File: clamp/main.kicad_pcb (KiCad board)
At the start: 2 copper layers, 37 parts, among them P1 CONN_01X12, U1 LM741, U2 LM741, U3 LM741, U4 LM741, U5 LM741, U6 LM741

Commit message: basic layout
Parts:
- added C14: C, Capacitors_SMD:C_1206, F.Cu at (116.2, 55.9)
- added C15: C, Capacitors_SMD:C_1206, F.Cu at (132.7, 66.0)
- added C16: C, Capacitors_SMD:C_1206, F.Cu at (119.4, 74.9)
- added C17: C, Capacitors_SMD:C_1206, F.Cu at (63.5, 62.2)
- added C18: C, Capacitors_SMD:C_1206, F.Cu at (76.8, 72.4)
- added C19: C, Capacitors_SMD:C_1206, F.Cu at (76.8, 57.1)
- added C20: C, Capacitors_SMD:C_1206, F.Cu at (88.3, 61.6)
- added C21: C, Capacitors_SMD:C_1206, F.Cu at (91.4, 66.7)
- added C22: C, Capacitors_SMD:C_1206, F.Cu at (91.4, 72.4)
- added C23: C, Capacitors_SMD:C_1206, F.Cu at (93.3, 79.4)
- added C24: C, Capacitors_SMD:C_1206, F.Cu at (94.0, 84.5)
- added C25: C, Capacitors_SMD:C_1206, F.Cu at (88.3, 90.2)
- added C26: C, Capacitors_SMD:C_1206, F.Cu at (243.2, 57.8)
- added C27: C, Capacitors_SMD:C_1206, F.Cu at (241.3, 43.8)
- added C28: C, Capacitors_SMD:C_1206, F.Cu at (237.5, 43.8)
- added C33: C, Capacitors_SMD:C_1206, F.Cu at (252.7, 57.8)
- added C34: C, Capacitors_SMD:C_1206, F.Cu at (249.6, 57.8)
- added D5: 1N4148, Diodes_ThroughHole:Diode_DO-35_SOD27_Horizontal_RM10, F.Cu at (179.7, 38.1)
- added D6: 1N4148, Diodes_ThroughHole:Diode_DO-35_SOD27_Horizontal_RM10, F.Cu at (183.5, 48.3)
- added D7: 1N4148, Diodes_ThroughHole:Diode_DO-35_SOD27_Horizontal_RM10, F.Cu at (247.0, 43.2)
- added P2: CONN_01X15, Pin_Headers:Pin_Header_Straight_1x15, F.Cu at (56.5, 73.7)
- added P3: CONN_01X03, Pin_Headers:Pin_Header_Straight_1x03, F.Cu at (69.2, 33.0)
- added P4: CONN_01X06, Pin_Headers:Pin_Header_Straight_1x06, F.Cu at (221.6, 43.8)
- added R15: R, Resistors_SMD:R_1206, F.Cu at (121.9, 61.0)
- added R20: 120, Resistors_ThroughHole:Resistor_Vertical_RM5mm, F.Cu at (230.5, 49.5)
- added R21: R, Resistors_ThroughHole:Resistor_Vertical_RM5mm, F.Cu at (237.5, 33.0)
- added U13: LM741, SMD_Packages:SOIC-8-N, F.Cu at (246.4, 50.2)
- added U7: LM741, Housings_SOIC:SOIC-8_3.9x4.9mm_Pitch1.27mm, F.Cu at (123.2, 67.3)
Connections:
- C1 pad 1: -VE -> +VE
- C2 pad 1: +VE -> -VE
- D2 pad 1: Net-(D2-Pad1) -> OUT
- D2 pad 2: OUT -> Net-(D2-Pad2)
- D3 pad 1: OUT -> Net-(D3-Pad1)
- D3 pad 2: Net-(D3-Pad2) -> OUT
- R10 pad 2: V-FB -> I-FB
- R11 pad 1: Net-(R10-Pad1) -> Net-(R11-Pad1)
- R11 pad 2: V-SET -> V-FB
- R12 pad 1: Net-(R12-Pad1) -> Net-(R11-Pad1)
- R12 pad 2: V-FB -> Net-(R12-Pad2)
- R13 pad 1: Net-(R12-Pad1) -> OUT
- R13 pad 2: Net-(R13-Pad2) -> REF
- R14 pad 1: -VE -> Net-(R14-Pad1)
- R14 pad 2: +VE -> REF
- R2 pad 2: Net-(R1-Pad1) -> V-SET
- R3 pad 2: I-FB -> Net-(R1-Pad1)
- R4 pad 1: Net-(R3-Pad1) -> Net-(R12-Pad2)
- R4 pad 2: I-SET -> Net-(R2-Pad1)
- R6 pad 2: Net-(R2-Pad1) -> I-SET
- R7 pad 1: OUT -> Net-(R7-Pad1)
- R7 pad 2: REF -> V-FB
- R8 pad 1: Net-(R8-Pad1) -> Net-(R7-Pad1)
- R9 pad 1: Net-(R13-Pad2) -> Net-(R10-Pad1)
- R9 pad 2: Net-(R8-Pad1) -> Net-(R3-Pad1)
- U1 pad 2: OUT -> Net-(R1-Pad1)
- U1 pad 3: Net-(R3-Pad1) -> GND
- U1 pad 6: Net-(D1-Pad2) -> Net-(R3-Pad1)
- U2 pad 2: Net-(R1-Pad1) -> Net-(R2-Pad1)
- U2 pad 6: Net-(R2-Pad1) -> Net-(R12-Pad2)
- U3 pad 6: Net-(D2-Pad1) -> Net-(D1-Pad2)
- U4 pad 2: Net-(R8-Pad1) -> OUT
- U4 pad 3: GND -> Net-(R10-Pad1)
- U4 pad 6: Net-(R13-Pad2) -> Net-(D4-Pad1)
- U5 pad 3: Net-(R10-Pad1) -> Net-(R7-Pad1)
- U5 pad 6: Net-(D3-Pad2) -> Net-(D2-Pad2)
- U6 pad 3: Net-(R12-Pad1) -> Net-(R11-Pad1)
- U6 pad 6: Net-(D4-Pad1) -> Net-(D3-Pad1)
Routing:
- net V-FB: track 52.3 -> 0.07 mm
- net OUT: track 216.8 -> 183.7 mm
- net I-FB: track 36.9 -> 12.5 mm
- net I-SET: track 35.7 -> 12.4 mm
- net Net-(R13-Pad2): track 21.5 -> 0.00 mm
- net V-SET: track 43.3 -> 23.5 mm
- net -VE: track 270.8 -> 251.6 mm, vias 9 -> 8
- net Net-(R8-Pad1): track 16.0 -> 0.00 mm
- net Net-(R2-Pad1): track 13.9 -> 0.00 mm
- net Net-(R12-Pad1): track 10.1 -> 0.00 mm
- net +VE: track 292.1 -> 283.3 mm, vias 8 -> 7
- net Net-(D2-Pad2): track 0.00 -> 8.79 mm
- net Net-(R11-Pad1): track 0.00 -> 7.11 mm
- net Net-(R10-Pad1): track 10.8 -> 5.44 mm, vias 0 -> 1
- net Net-(R3-Pad1): track 9.36 -> 4.31 mm
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
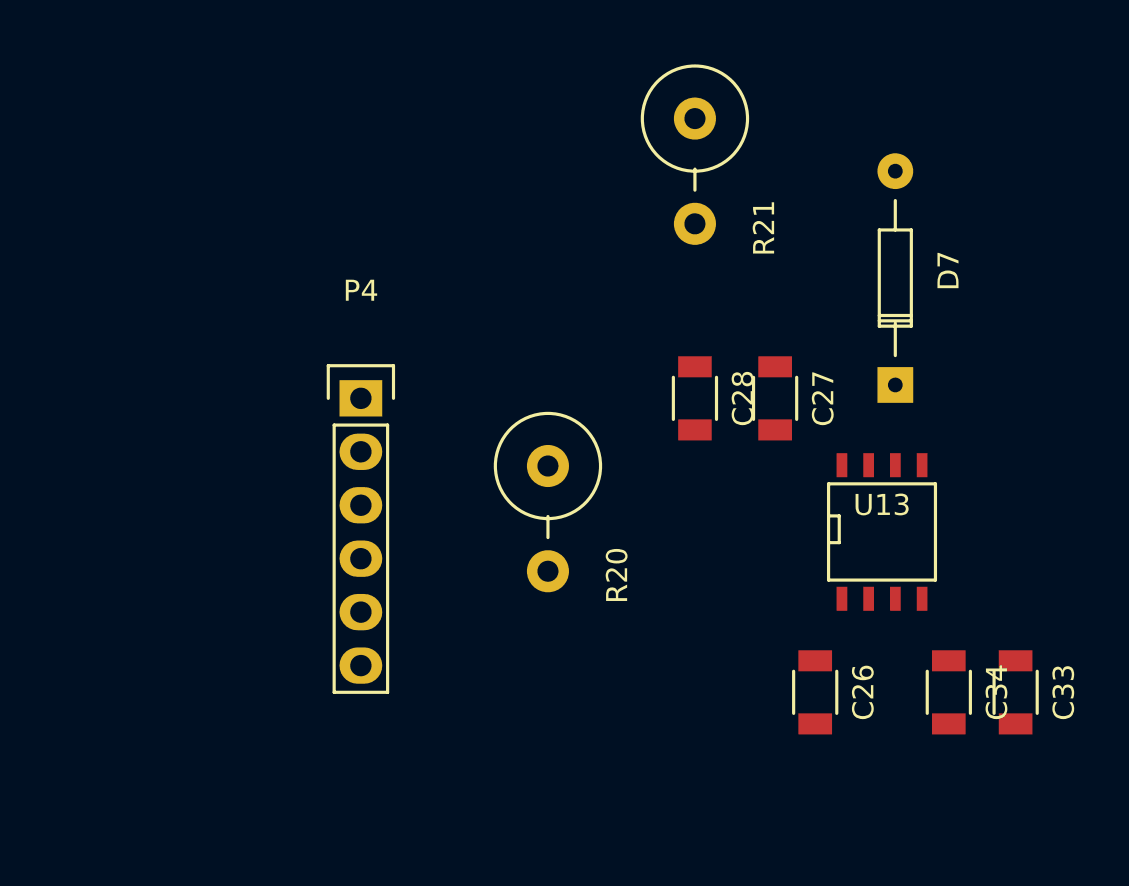
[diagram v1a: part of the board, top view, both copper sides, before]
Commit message: new footprint to-5
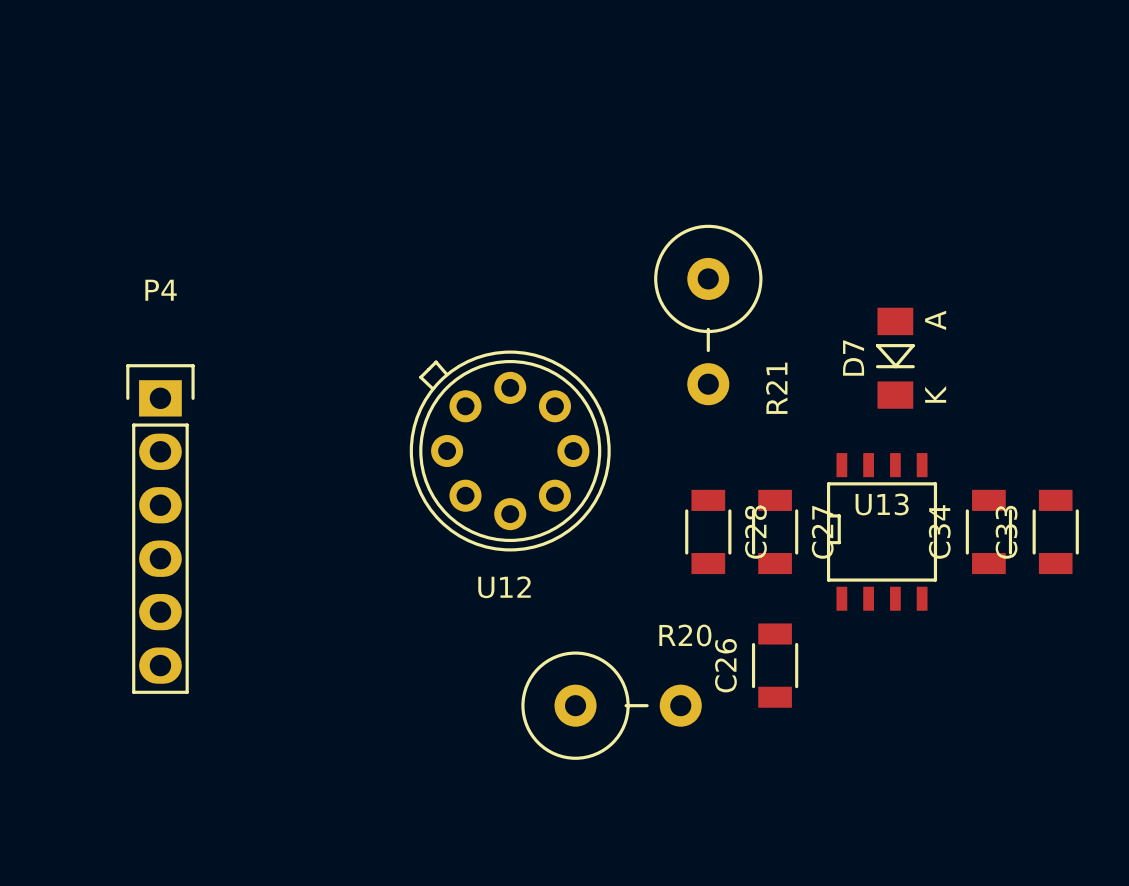
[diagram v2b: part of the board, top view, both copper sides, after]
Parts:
- added U12: LTZ1000, footprint:TO-5_Housing_8Pin, F.Cu at (228.6, 46.4)
- D7: footprint Diodes_ThroughHole:Diode_DO-35_SOD27_Horizontal_RM10 -> Diodes_SMD:MiniMELF_Standard
- moved R20 9.67 mm to (234.3, 58.4), turned to 0 degrees
- moved P4 9.53 mm to (212.1, 43.8)
- moved C33 7.85 mm to (254.6, 50.2), turned to 90 degrees
- moved C34 7.85 mm to (251.5, 50.2), turned to 90 degrees
- moved R21 7.65 mm to (238.1, 40.6)
- moved C28 6.38 mm to (238.1, 50.2)
- moved C27 6.35 mm to (241.3, 50.2)
- moved C26 2.29 mm to (241.3, 56.5), turned to 90 degrees
- moved D7 1.27 mm to (247.0, 41.9)

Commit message: pcb for first bit
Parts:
- R20, R21: footprint Resistors_ThroughHole:Resistor_Vertical_RM5mm -> Resistors_ThroughHole:Resistor_TO-220_Vertical
- moved R21 22.7 mm to (215.9, 45.1)
- moved R20 14.7 mm to (219.7, 57.1), turned to 270 degrees
- moved C26 4.49 mm to (245.7, 57.1), turned to 180 degrees
- moved P4 2.54 mm to (209.6, 43.8)
- turned U12 to 90 degrees
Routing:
- net GND: track 45.5 -> 152.6 mm, vias 8 -> 12
- net -VE: track 251.6 -> 325.3 mm, vias 8 -> 9
- net Net-(C26-Pad1): track 0.00 -> 71.0 mm
- net REF: track 0.69 -> 54.6 mm
- net +VE: track 283.3 -> 331.3 mm, vias 7 -> 8
- net Net-(R20-Pad1): track 0.00 -> 34.4 mm
- net Net-(D7-Pad1): track 0.00 -> 3.33 mm

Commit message: update
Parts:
- added C29: 0.1uF, Capacitors_SMD:C_1206, F.Cu at (187.3, 60.3)
- added C30: 0.1uF, Capacitors_SMD:C_1206, F.Cu at (207.6, 57.8)
- added D8: 1N4148, Diodes_SMD:MiniMELF_Standard, F.Cu at (211.5, 57.8)
- added Q1: 2N3904, TO_SOT_Packages_SMD:SOT-23, F.Cu at (186.7, 47.6)
- added R22: 1k, Resistors_SMD:R_1206, F.Cu at (192.4, 46.4)
- added R23: 1M, Resistors_SMD:R_1206, F.Cu at (192.4, 59.7)
- added R24: 10k, Resistors_SMD:R_1206, F.Cu at (196.2, 45.7)
- added RV1: POT, Potentiometers:Potentiometer_Bourns_3296Y_3-8Zoll_Angular_ScrewUp, F.Cu at (201.9, 47.0)
- added U14: LM741, SMD_Packages:SOIC-8-N, F.Cu at (193.0, 52.7)
- added r1: 70k, Resistors_ThroughHole:Resistor_TO-220_Vertical, F.Cu at (215.3, 46.4)
- C26: value C -> 22nF
- R21: value R -> 70k
- moved C33 56.6 mm to (198.1, 52.7)
- moved C28 50.2 mm to (188.0, 52.7)
- moved D5 47.0 mm to (132.7, 38.7)
- moved D6 45.1 mm to (138.4, 48.9)
- moved P4 11.9 mm to (214.6, 33.0), turned to 270 degrees
- moved R21 7.73 mm to (208.3, 46.4)
- moved R20 4.45 mm to (215.3, 57.1)
- moved C27 3.18 mm to (238.1, 50.2)
- turned U12 to 270 degrees
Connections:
- R21 pad 2: Net-(C26-Pad1) -> Net-(C30-Pad1)
- U12 pad 1: (no net) -> Net-(C29-Pad2)
- U12 pad 2: (no net) -> Net-(D8-Pad1)
- U12 pad 6: (no net) -> Net-(R24-Pad2)
- U12 pad 8: (no net) -> Net-(C30-Pad1)
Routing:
- net -VE: track 325.3 -> 420.3 mm, vias 9 -> 11
- net +VE: track 331.3 -> 390.2 mm, vias 8 -> 10
- net GND: track 152.6 -> 205.8 mm, vias 12 -> 20
- net Net-(C30-Pad1): track 0.00 -> 44.2 mm
- net Net-(R24-Pad2): track 0.00 -> 32.6 mm
- net REF: track 54.6 -> 77.4 mm, vias 0 -> 2
- net Net-(R23-Pad1): track 0.00 -> 13.8 mm
- net Net-(C26-Pad1): track 71.0 -> 57.5 mm
- net Net-(C29-Pad2): track 0.00 -> 13.3 mm
- net Net-(C29-Pad1): track 0.00 -> 3.92 mm
- net Net-(Q1-Pad2): track 0.00 -> 3.40 mm
- net Net-(R22-Pad1): track 0.00 -> 3.25 mm
- net Net-(R20-Pad1): track 34.4 -> 32.1 mm
- net (no net): track 0.00 -> 1.80 mm

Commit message: update
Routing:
- net Net-(D8-Pad1): track 0.00 -> 20.1 mm
- net GND: track 205.8 -> 209.5 mm, vias 20 -> 19
- net Net-(C26-Pad1): track 57.5 -> 59.5 mm

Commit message: update
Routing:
- net Net-(C29-Pad2): track 13.3 -> 59.6 mm
- net Net-(D8-Pad1): track 20.1 -> 0.15 mm
- net +VE: track 390.0 -> 393.5 mm
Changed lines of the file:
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@@
   (general
     (links 167)
-    (no_connects 86)
+    (no_connects 87)
     (area 51.181667 26.645 257.270002 151.352002)
     (thickness 1.6)
     (drawings 13)
-    (tracks 478)
+    (tracks 490)
     (zones 0)
     (modules 76)
@@
   )
   (segment (start 181.61 40.005) (end 180.34 41.275) (width 0.75) (layer B.Cu) (net 0))
-  (segment (start 240.03 46.355) (end 240.03 48.665) (width 0.75) (layer F.Cu) (net 1))
+  (segment (start 237.49 40.005) (end 244.475 40.005) (width 0.75) (layer B.Cu) (net 1))
+  (segment (start 245.379998 45.72) (end 246.014998 46.355) (width 0.75) (layer F.Cu) (net 1))
+  (segment (start 245.11 45.72) (end 245.379998 45.72) (width 0.75) (layer F.Cu) (net 1))
+  (segment (start 244.475 45.085) (end 245.11 45.72) (width 0.75) (layer F.Cu) (net 1))
+  (segment (start 244.475 42.545) (end 244.475 45.085) (width 0.75) (layer F.Cu) (net 1))
+  (via (at 244.475 42.545) (size 1.75) (drill 0.75) (layers F.Cu B.Cu) (net 1))
+  (segment (start 244.475 40.005) (end 244.475 42.545) (width 0.75) (layer B.Cu) (net 1))
   (segment (start 240.03 48.665) (end 240.03 48.895) (width 0.75) (layer F.Cu) (net 1))
   (segment (start 240.03 48.895) (end 240.03 48.665) (width 0.75) (layer F.Cu) (net 1))
@@
   (segment (start 213.36 40.005) (end 213.995 40.005) (width 0.75) (layer B.Cu) (net 1))
   (segment (start 213.995 40.005) (end 237.49 40.005) (width 0.75) (layer B.Cu) (net 1))
-  (segment (start 237.49 40.005) (end 240.03 40.64) (width 0.75) (layer B.Cu) (net 1))
-  (segment (start 240.03 40.64) (end 240.03 46.355) (width 0.75) (layer B.Cu) (net 1))
-  (via (at 240.03 46.355) (size 1.75) (drill 0.75) (layers F.Cu B.Cu) (net 1))
   (segment (start 213.36 40.005) (end 214.63 33.02) (width 0.75) (layer B.Cu) (net 1) (status 20))
   (segment (start 245.745 48.895) (end 241.53 48.895) (width 0.75) (layer F.Cu) (net 1))
@@
   (segment (start 219.4075 44.1175) (end 217.805 45.72) (width 0.75) (layer F.Cu) (net 33))
   (segment (start 196.215 44.45) (end 196.215 44.27) (width 0.75) (layer F.Cu) (net 33))
+  (segment (start 228.6 57.785) (end 211.455 57.785) (width 0.75) (layer F.Cu) (net 34))
+  (segment (start 189.865 58.42) (end 191.135 59.69) (width 0.75) (layer F.Cu) (net 34))
+  (segment (start 191.135 59.69) (end 201.93 59.69) (width 0.75) (layer F.Cu) (net 34))
+  (segment (start 201.93 59.69) (end 203.2 60.96) (width 0.75) (layer F.Cu) (net 34))
+  (segment (start 203.2 60.96) (end 208.915 60.96) (width 0.75) (layer F.Cu) (net 34))
+  (segment (start 208.915 60.96) (end 209.55 60.325) (width 0.75) (layer F.Cu) (net 34))
+  (segment (start 209.55 60.325) (end 209.55 58.42) (width 0.75) (layer F.Cu) (net 34))
+  (segment (start 209.55 58.42) (end 210.185 57.785) (width 0.75) (layer F.Cu) (net 34))
+  (segment (start 210.185 57.785) (end 211.455 57.785) (width 0.75) (layer F.Cu) (net 34))
+  (segment (start 189.865 58.42) (end 185.825 58.42) (width 0.75) (layer F.Cu) (net 34))
   (segment (start 187.69076 48.575) (end 187.05576 48.575) (width 0.75) (layer F.Cu) (net 34))
   (segment (start 187.05576 48.575) (end 185.78576 49.845) (width 0.75) (layer F.Cu) (net 34))
@@
   (segment (start 185.78576 49.79924) (end 186.055 49.53) (width 0.75) (layer F.Cu) (net 34))
   (segment (start 185.78576 49.845) (end 185.78576 53.60924) (width 0.75) (layer F.Cu) (net 34))
-  (segment (start 185.825 54.205) (end 185.825 60.325) (width 0.75) (layer F.Cu) (net 34))
+  (segment (start 185.825 54.205) (end 185.825 58.42) (width 0.75) (layer F.Cu) (net 34))
+  (segment (start 185.825 58.42) (end 185.825 60.325) (width 0.75) (layer F.Cu) (net 34))
   (segment (start 185.78576 53.60924) (end 185.825 54.205) (width 0.75) (layer F.Cu) (net 34))
   (segment (start 211.455 56.03494) (end 211.60994 56.03494) (width 0.75) (layer F.Cu) (net 35))
-  (segment (start 211.60994 56.03494) (end 212.725 57.15) (width 0.75) (layer F.Cu) (net 35))
-  (segment (start 212.725 57.15) (end 231.14 57.15) (width 0.75) (layer F.Cu) (net 35))
   (segment (start 226.4375 48.3675) (end 218.5475 48.3675) (width 0.75) (layer F.Cu) (net 36))
   (segment (start 209.55 46.99) (end 208.28 48.26) (width 0.75) (layer F.Cu) (net 36))

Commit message: update
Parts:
- moved U12 0.90 mm to (228.0, 45.7)
- moved C27 0.63 mm to (238.8, 50.2)
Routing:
- net Net-(D8-Pad1): track 0.15 -> 29.6 mm, vias 0 -> 2
- net REF: track 77.4 -> 104.5 mm
- net Net-(R20-Pad1): track 32.1 -> 48.2 mm, vias 0 -> 2
- net Net-(C29-Pad2): track 59.6 -> 69.1 mm, vias 0 -> 2
- net +VE: track 393.5 -> 402.5 mm
- net GND: track 209.5 -> 213.3 mm
- net Net-(C26-Pad1): track 59.5 -> 61.8 mm
- net Net-(R24-Pad2): track 32.6 -> 32.0 mm
- net Net-(C30-Pad1): track 44.2 -> 43.5 mm

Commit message: update
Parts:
- moved C34 1.91 mm to (249.6, 50.2)
- moved C27 1.27 mm to (240.0, 50.2)
- moved D7 1.27 mm to (245.7, 41.9)
- moved U13 1.27 mm to (245.1, 50.2)
- moved C26 0.63 mm to (245.1, 57.1)
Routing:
- net REF: track 104.5 -> 86.2 mm
- net (no net): track 1.80 -> 18.8 mm
- net GND: track 213.3 -> 219.9 mm
- net -VE: track 420.3 -> 413.7 mm
- net +VE: track 402.5 -> 398.1 mm
- net Net-(C26-Pad1): track 61.8 -> 60.8 mm
- net Net-(R20-Pad1): track 48.2 -> 47.7 mm
